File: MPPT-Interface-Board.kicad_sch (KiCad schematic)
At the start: 12 parts, among them J1 MPPT CAN 1, J2 MPPT CAN 2, J3 CarCAN 1, J4 CarCAN 2, J5 FUSEBOX, U1 RI3-1209S

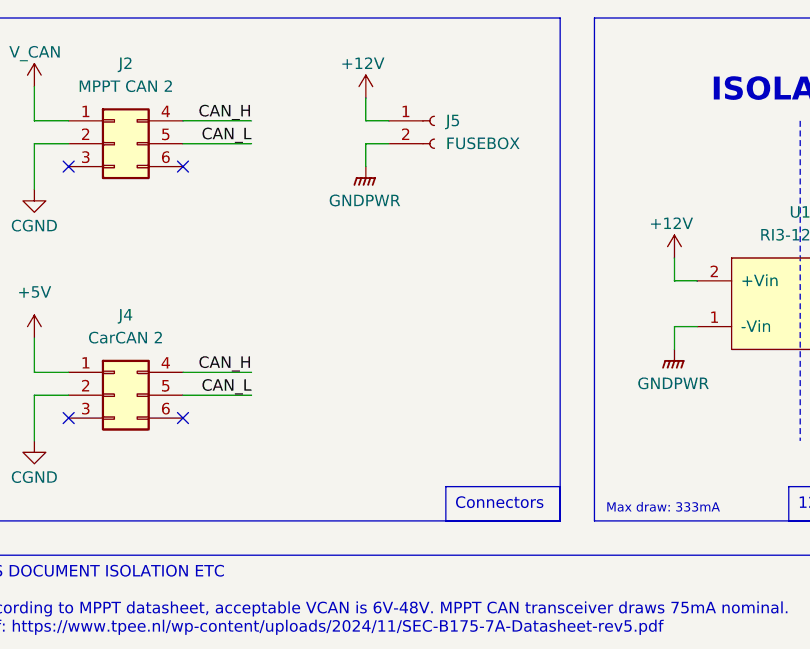
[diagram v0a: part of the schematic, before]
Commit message: add candapter conn
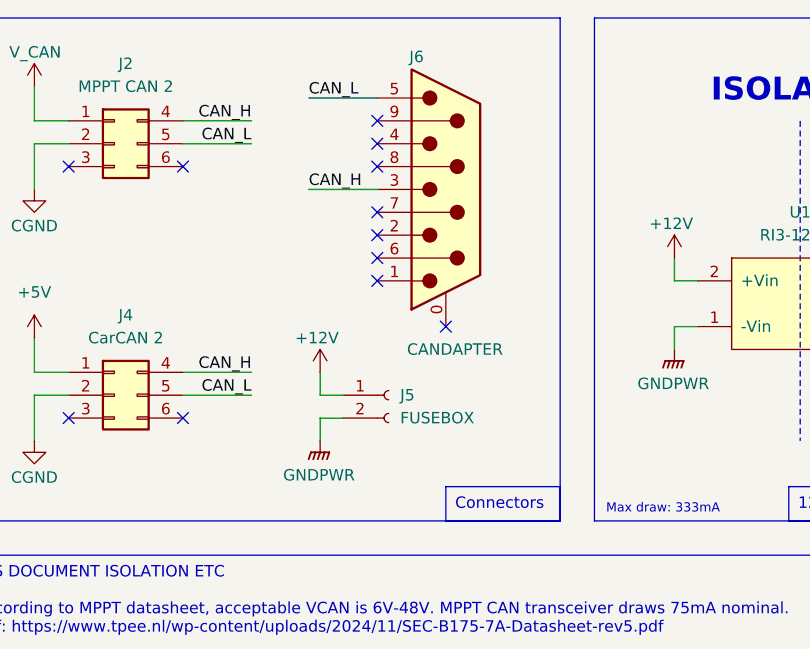
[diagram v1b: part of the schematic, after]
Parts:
- added J6: CANDAPTER, DB-9 Connector:AMPHENOL_L77SDE09SA4CH3R, symbol Connector:DE9_Plug_MountingHoles
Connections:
- net CAN_H: now also J6.3
- net CAN_L: now also J6.5
- no-connect marks 8 -> 16
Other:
- moved on the sheet: J5
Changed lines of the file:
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@@
+	)
+	(no_connect
+		(at 93.98 45.72)
 	)
 	(no_connect
@@
 	)
 	(no_connect
+		(at 93.98 48.26)
+	)
+	(no_connect
 		(at 72.39 63.5)
 	)
@@
 	)
 	(no_connect
+		(at 93.98 33.02)
+	)
+	(no_connect
+		(at 93.98 30.48)
+	)
+	(no_connect
 		(at 27.94 63.5)
 	)
@@
 		(at 40.64 63.5)
 	)
-	(wire
-		(pts
-			(xy 92.71 33.02) (xy 92.71 35.56)
+	(no_connect
+		(at 93.98 43.18)
+	)
+	(no_connect
+		(at 93.98 35.56)
+	)
+	(no_connect
+		(at 93.98 40.64)
+	)
+	(no_connect
+		(at 101.6 53.34)
+	)
+	(wire
+		(pts
+			(xy 87.63 63.5) (xy 87.63 66.04)
 		)
 		(stroke
@@
 	(wire
 		(pts
-			(xy 92.71 30.48) (xy 95.25 30.48)
+			(xy 87.63 60.96) (xy 90.17 60.96)
 		)
 		(stroke
@@
 	(wire
 		(pts
-			(xy 92.71 27.94) (xy 92.71 30.48)
+			(xy 87.63 58.42) (xy 87.63 60.96)
 		)
 		(stroke
@@
 	(wire
 		(pts
+			(xy 86.36 27.94) (xy 93.98 27.94)
+		)
+		(stroke
+			(width 0)
+			(type default)
+		)
+	)
+	(wire
+		(pts
 			(xy 40.64 30.48) (xy 48.26 30.48)
 		)
@@
 	(wire
 		(pts
+			(xy 86.36 38.1) (xy 93.98 38.1)
+		)
+		(stroke
+			(width 0)
+			(type default)
+		)
+	)
+	(wire
+		(pts
 			(xy 222.25 60.96) (xy 222.25 63.5)
 		)
@@
 	(wire
 		(pts
-			(xy 95.25 33.02) (xy 92.71 33.02)
+			(xy 90.17 63.5) (xy 87.63 63.5)
 		)
 		(stroke
@@
 		)
 	)
+	(label "CAN_H"
+		(at 86.36 38.1 0)
+		(fields_autoplaced yes)
+		(effects
+			(font
+				(size 1.27 1.27)
+			)
+			(justify left bottom)
+		)
+	)
 	(label "CAN_L"
 		(at 48.26 60.96 180)
@@
 		)
 	)
+	(label "CAN_L"
+		(at 86.36 27.94 0)
+		(fields_autoplaced yes)
+		(effects
+			(font
+				(size 1.27 1.27)
+			)
+			(justify left bottom)
+		)
+	)
 	(symbol
 		(lib_id "Connector_Generic:Conn_02x03_Top_Bottom")
@@
 	(symbol
 		(lib_id "Connector:Conn_01x02_Socket")
-		(at 100.33 30.48 0)
+		(at 95.25 60.96 0)
 		(unit 1)
 		(exclude_from_sim no)
@@
 		(dnp no)
 		(property "Reference" "J5"
-			(at 101.6 30.4799 0)
+			(at 96.52 60.9599 0)
 			(effects
 				(font
@@
 		)
 		(property "Value" "FUSEBOX"
-			(at 101.6 33.02 0)
+			(at 96.52 63.5 0)
 			(effects
 				(font
@@
 		)
 		(property "Footprint" "Connector_Molex:Molex_Micro-Fit_3.0_43650-0215_1x02_P3.00mm_Vertical"
-			(at 100.33 30.48 0)
+			(at 95.25 60.96 0)
 			(effects
 				(font
@@
 		)
 		(property "Datasheet" "~"
-			(at 100.33 30.48 0)
+			(at 95.25 60.96 0)
 			(effects
 				(font
@@
 		)
 		(property "Description" "Generic connector, single row, 01x02, script generated"
-			(at 100.33 30.48 0)
+			(at 95.25 60.96 0)
 			(effects
 				(font
@@
 		)
 		(property "P/N" "0436500215"
-			(at 100.33 30.48 0)
+			(at 95.25 60.96 0)
 			(effects
 				(font
@@
 		)
 		(property "Sim.Device" ""
-			(at 100.33 30.48 0)
+			(at 95.25 60.96 0)
 			(effects
 				(font
@@
 		)
 		(property "Sim.Pins" ""
-			(at 100.33 30.48 0)
+			(at 95.25 60.96 0)
 			(effects
 				(font
@@
 	)
 	(symbol
+		(lib_id "Connector:DE9_Plug_MountingHoles")
+		(at 101.6 38.1 0)
+		(unit 1)
+		(exclude_from_sim no)
+		(in_bom yes)
+		(on_board yes)
+		(dnp no)
+		(property "Reference" "J6"
+			(at 97.536 23.368 0)
+			(effects
+				(font
+					(size 1.27 1.27)
+				)
+				(justify left)
+			)
+		)
+		(property "Value" "CANDAPTER"
+			(at 97.282 55.88 0)
+			(effects
+				(font
+					(size 1.27 1.27)
+				)
+				(justify left)
+			)
+		)
+		(property "Footprint" "DB-9 Connector:AMPHENOL_L77SDE09SA4CH3R"
+			(at 101.6 38.1 0)
+			(effects
+				(font
+					(size 1.27 1.27)
+				)
+				(hide yes)
+			)
+		)
+		(property "Datasheet" "https://cdn.amphenol-cs.com/media/wysiwyg/files/drawing/l77sdxxxsa4ch3r.pdf"
+			(at 101.6 38.1 0)
+			(effects
+				(font
+					(size 1.27 1.27)
+				)
+				(hide yes)
+			)
+		)
+		(property "Description" "9-pin male plug pin D-SUB connector, Mounting Hole"
+			(at 101.6 38.1 0)
+			(effects
+				(font
+					(size 1.27 1.27)
+				)
+				(hide yes)
+			)
+		)
+		(property "P/N" "L77SDE09SA4CH3R"
+			(at 101.6 38.1 0)
+			(effects
+				(font
+					(size 1.27 1.27)
+				)
+				(hide yes)
+			)
+		)
+		(property "Sim.Device" ""
+			(at 101.6 38.1 0)
+			(effects
+				(font
+					(size 1.27 1.27)
+				)
+				(hide yes)
+			)
+		)
+		(property "Sim.Pins" ""
+			(at 101.6 38.1 0)
+			(effects
+				(font
+					(size 1.27 1.27)
+				)
+				(hide yes)
+			)
+		)
+		(pin "1"
+		)
+		(pin "8"
+		)
+		(pin "2"
+		)
+		(pin "6"
+		)
+		(pin "9"
+		)
+		(pin "7"
+		)
+		(pin "4"
+		)
+		(pin "5"
+		)
+		(pin "3"
+		)
+		(pin "0"
+		)
+		(instances
+			(project "MPPT-Interface-Board"
+				(path "/b7de5949-1fc3-44b6-95a7-0faccc8a2b33"
+					(reference "J6")
+					(unit 1)
+				)
+			)
+		)
+	)
+	(symbol
 		(lib_id "power:GND")
 		(at 24.13 38.1 0)
@@
 	(symbol
 		(lib_id "power:GNDPWR")
-		(at 92.71 35.56 0)
+		(at 87.63 66.04 0)
 		(unit 1)
 		(exclude_from_sim no)
@@
 		(fields_autoplaced yes)
 		(property "Reference" "#PWR02"
-			(at 92.71 40.64 0)
+			(at 87.63 71.12 0)
 			(effects
 				(font
@@
 		)
 		(property "Value" "GNDPWR"
-			(at 92.583 39.37 0)
+			(at 87.503 69.85 0)
 			(effects
 				(font
@@
 		)
 		(property "Footprint" ""
-			(at 92.71 36.83 0)
+			(at 87.63 67.31 0)
 			(effects
 				(font
@@
 		)
 		(property "Datasheet" ""
-			(at 92.71 36.83 0)
+			(at 87.63 67.31 0)
 			(effects
 				(font
@@
 		)
 		(property "Description" "Power symbol creates a global label with name \"GNDPWR\" , global ground"
-			(at 92.71 35.56 0)
+			(at 87.63 66.04 0)
 			(effects
 				(font
@@
 	(symbol
 		(lib_id "power:+12V")
-		(at 92.71 27.94 0)
+		(at 87.63 58.42 0)
 		(unit 1)
 		(exclude_from_sim no)
@@
 		(dnp no)
 		(property "Reference" "#PWR03"
-			(at 92.71 31.75 0)
+			(at 87.63 62.23 0)
 			(effects
 				(font
@@
 		)
 		(property "Value" "+12V"
-			(at 89.916 24.13 0)
+			(at 84.836 54.61 0)
 			(effects
 				(font
@@
 		)
 		(property "Footprint" ""
-			(at 92.71 27.94 0)
+			(at 87.63 58.42 0)
 			(effects
 				(font
@@
 		)
 		(property "Datasheet" ""
-			(at 92.71 27.94 0)
+			(at 87.63 58.42 0)
 			(effects
 				(font
@@
 		)
 		(property "Description" "Power symbol creates a global label with name \"+12V\""
-			(at 92.71 27.94 0)
-			(effects
-				(font
+			(at 87.63 58.42 0)
+			(effects
+				(font

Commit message: add RPP
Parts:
- added C5: 10u, Capacitor_SMD:C_0805_2012Metric, symbol Device:C_Small
- added D1: SD12_SOD323, Diode_SMD:D_SOD-323, symbol Diode:SD12_SOD323
- added Q1: PMV35EPER, Package_TO_SOT_SMD:SOT-23, symbol utsvt-chips:PMV35EPE
- added R2: 100k, Resistor_SMD:R_0805_2012Metric, symbol Device:R_Small
- added Z1: BZT52-B12-QX, Zener:BZT52B12QX, symbol BZT52-B12-QX:BZT52-B12-QX
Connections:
- net +12V: now also D1.2 (A2), Q1.3 (D); no longer U1.2 (+Vin)
- net GNDPWR: now also C5.2, D1.1 (A1), R2.1
- new net: Q1.1 (G), R2.2, Z1.2 (A)
- new net +12V_PROT: C5.1, Q1.2 (S), U1.2 (+Vin), Z1.1 (K)
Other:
- moved on the sheet: C1, C2, C3, C4, U1

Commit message: fix loop?
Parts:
- removed J2: MPPT CAN 2, Connector_Molex:Molex_Micro-Fit_3.0_43045-0612_2x03_P3.00mm_Vertical, symbol Connector_Generic:Conn_02x03_Top_Bottom
- removed J5: FUSEBOX, Connector_Molex:Molex_Micro-Fit_3.0_43650-0215_1x02_P3.00mm_Vertical, symbol Connector:Conn_01x02_Socket
- added J2: MPPT CAN 2, Connector_Molex:Molex_Micro-Fit_3.0_43650-0215_1x02_P3.00mm_Vertical, symbol Connector_Generic:Conn_01x02
- added J5: FUSEBOX, Connector_Molex:Molex_Micro-Fit_3.0_43650-0215_1x02_P3.00mm_Vertical, symbol Connector_Generic:Conn_01x02
- added TP1, TP6: CGND, symbol Connector:TestPoint
- added TP2: GNDPWR, symbol Connector:TestPoint
- added TP3: 5V, symbol Connector:TestPoint
- added TP4: 12V, symbol Connector:TestPoint
- added TP5: VCAN, symbol Connector:TestPoint
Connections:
- net +12V: now also J5.1 (Pin_1)
- net +12V_PROT: now also TP4.1
- net +5V: now also TP3.1
- net CAN_H: now also J2.1 (Pin_1)
- net CAN_L: now also J2.2 (Pin_2)
- net CGND: now also TP1.1, TP6.1
- net GNDPWR: now also J5.2 (Pin_2), TP2.1
- net V_CAN: now also TP5.1
- no-connect marks 16 -> 14

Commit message: add indicator LEDs
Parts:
- added D2: 12V, LED_SMD:LED_0805_2012Metric, symbol Device:LED
- added D3: 5V, LED_SMD:LED_0805_2012Metric, symbol Device:LED
- added D4: VCAN, LED_SMD:LED_0805_2012Metric, symbol Device:LED
- added R3: 22.1k, Resistor_SMD:R_0805_2012Metric, symbol Device:R
- added R4, R5: TODO, Resistor_SMD:R_0805_2012Metric, symbol Device:R
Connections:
- net +12V_PROT: now also R3.1
- net +5V: now also R4.1
- net CGND: now also D3.1 (K), D4.1 (K)
- net GNDPWR: now also D2.1 (K)
- net V_CAN: now also R5.1
- new net: D4.2 (A), R5.2
- new net: D3.2 (A), R4.2
- new net: D2.2 (A), R3.2
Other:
- moved on the sheet: C1, C2, C3, C4, TP1, TP2, TP3, TP4, TP5, TP6

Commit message: more fixes
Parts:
- removed J2: MPPT CAN 2, Connector_Molex:Molex_Micro-Fit_3.0_43650-0215_1x02_P3.00mm_Vertical, symbol Connector_Generic:Conn_01x02
- added J2: MPPT X, Connector_Molex:Molex_Micro-Fit_3.0_43045-0612_2x03_P3.00mm_Vertical, symbol Connector_Generic:Conn_02x03_Top_Bottom
- J1: value MPPT CAN 1 -> MPPT A
- J3: value CarCAN 1 -> CarCAN In
- J4: value CarCAN 2 -> CarCAN Out
- R3: value 22.1k -> 5.1k
- R4: value TODO -> 1.69k
- R5: value TODO -> 3.48k
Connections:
- net CAN_H: no longer J4.4 (Pin_4)
- net CAN_L: no longer J4.5 (Pin_5)
- net CGND: no longer J4.2 (Pin_2)
- net V_CAN: now also J2.1 (Pin_1)
- new net CAN_H2: J2.4 (Pin_4), J4.4 (Pin_4)
- new net CAN_L2: J2.5 (Pin_5), J4.5 (Pin_5)
- new net CGND2: J2.2 (Pin_2), J4.2 (Pin_2)
- no-connect marks 14 -> 16

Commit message: P/N for everything
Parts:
- C1, C2: value 10uF -> 10u
- C3: P/N (none) -> 08053A331JAT2A
- C4: P/N (none) -> 08053C471JAT2A
- C5: P/N C0805C105K3PACTU -> TMK212BBJ106MGHT
- J5: P/N (none) -> 0436500215
- R3: P/N CRCW080522K1FKEA -> RCA08055K10FKEA
- R4: P/N CRCW080522K1FKEA -> CRCW08051K69FKEA
- R5: P/N CRCW080522K1FKEA -> CRCW08053K48FKEA
- U1: P/N (none) -> RI3-1209S
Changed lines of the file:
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@@
 			)
 		)
+		(property "P/N" ""
+			(at 96.52 96.52 0)
+			(effects
+				(font
+					(size 1.27 1.27)
+				)
+				(hide yes)
+			)
+		)
 		(pin "1"
 		)
@@
 			)
 		)
+		(property "P/N" "0436500215"
+			(at 95.25 60.96 0)
+			(effects
+				(font
+					(size 1.27 1.27)
+				)
+				(hide yes)
+			)
+		)
 		(pin "1"
 		)
@@
 			)
 		)
+		(property "P/N" "RI3-1209S"
+			(at 198.12 44.45 0)
+			(effects
+				(font
+					(size 1.27 1.27)
+				)
+				(hide yes)
+			)
+		)
 		(pin "1"
 		)
@@
 			)
 		)
-		(property "P/N" "CRCW080522K1FKEA"
+		(property "P/N" "CRCW08051K69FKEA"
 			(at 139.7 92.71 0)
 			(effects
@@
 			)
 		)
+		(property "P/N" "08053C471JAT2A"
+			(at 210.82 88.9 0)
+			(effects
+				(font
+					(size 1.27 1.27)
+				)
+				(hide yes)
+			)
+		)
 		(pin "2"
 		)
@@
 			)
 		)
-		(property "Value" "10uF"
+		(property "Value" "10u"
 			(at 185.8772 96.393 0)
 			(effects
@@
 			)
 		)
-		(property "Value" "10uF"
+		(property "Value" "10u"
 			(at 174.4472 96.393 0)
 			(effects
@@
 			)
 		)
+		(property "P/N" ""
+			(at 31.75 87.63 0)
+			(effects
+				(font
+					(size 1.27 1.27)
+				)
+				(hide yes)
+			)
+		)
 		(pin "1"
 		)
@@
 			)
 		)
+		(property "P/N" ""
+			(at 86.36 96.52 0)
+			(effects
+				(font
+					(size 1.27 1.27)
+				)
+				(hide yes)
+			)
+		)
 		(pin "1"
 		)
@@
 			)
 		)
+		(property "P/N" ""
+			(at 106.68 96.52 0)
+			(effects
+				(font
+					(size 1.27 1.27)
+				)
+				(hide yes)
+			)
+		)
 		(pin "1"
 		)
@@
 			)
 		)
-		(property "P/N" "CRCW080522K1FKEA"
+		(property "P/N" "RCA08055K10FKEA"
 			(at 128.27 92.71 0)
 			(effects
@@
 			)
 		)
+		(property "P/N" ""
+			(at 73.66 95.25 0)
+			(effects
+				(font
+					(size 1.27 1.27)
+				)
+				(hide yes)
+			)
+		)
 		(pin "1"
 		)
@@
 			)
 		)
+		(property "P/N" ""
+			(at 63.5 95.25 0)
+			(effects
+				(font
+					(size 1.27 1.27)
+				)
+				(hide yes)
+			)
+		)
 		(pin "1"
 		)
@@
 			)
 		)
+		(property "P/N" "08053A331JAT2A"
+			(at 210.82 100.33 0)
+			(effects
+				(font
+					(size 1.27 1.27)
+				)
+				(hide yes)
+			)
+		)
 		(pin "2"
 		)
@@
 			)
 		)
+		(property "P/N" ""
+			(at 53.34 95.25 0)
+			(effects
+				(font
+					(size 1.27 1.27)
+				)
+				(hide yes)
+			)
+		)
 		(pin "1"
 		)
@@
 			)
 		)
-		(property "P/N" "C0805C105K3PACTU"
+		(property "P/N" "TMK212BBJ106MGHT"
 			(at 156.21 46.99 0)
 			(effects
@@
 			)
 		)
-		(property "P/N" "CRCW080522K1FKEA"
+		(property "P/N" "CRCW08053K48FKEA"
 			(at 149.86 92.71 0)
 			(effects

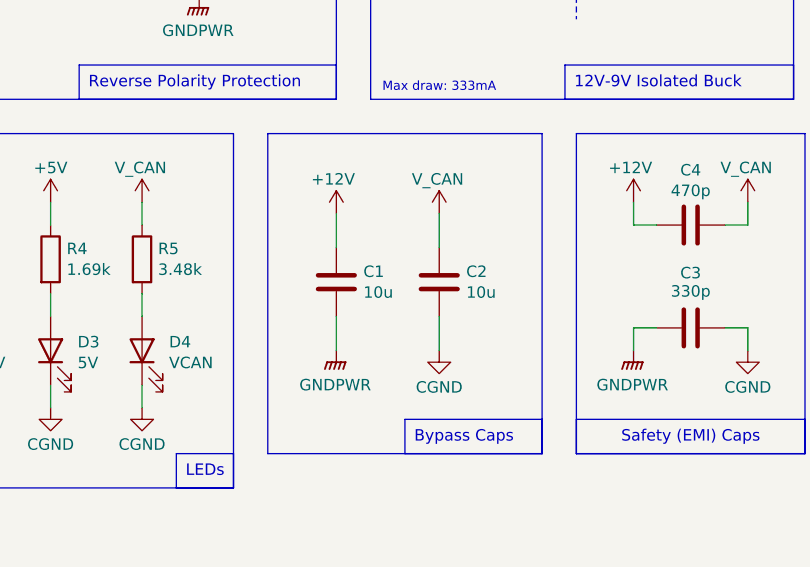
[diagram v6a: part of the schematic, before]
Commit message: fix bypass cap
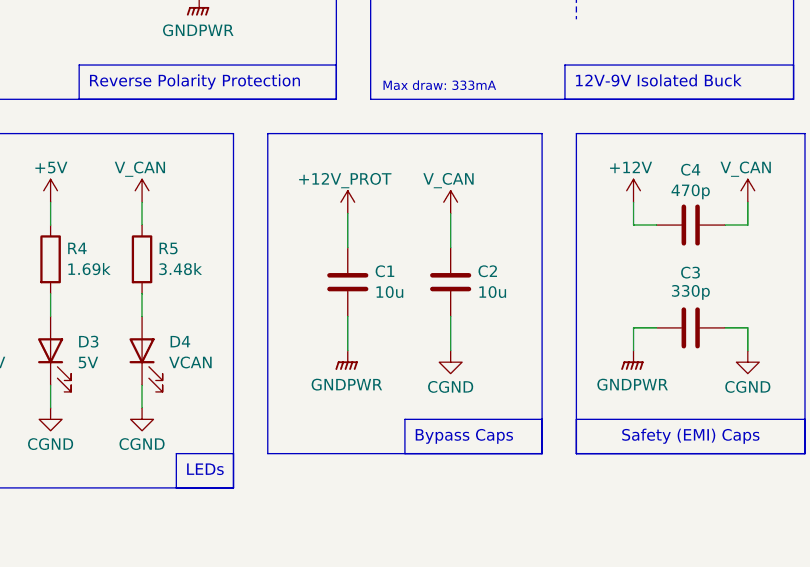
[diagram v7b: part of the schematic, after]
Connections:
- net +12V: no longer C1.1
- net +12V_PROT: now also C1.1
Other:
- moved on the sheet: C1, C2
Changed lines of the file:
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@@
 	(wire
 		(pts
-			(xy 182.88 99.06) (xy 182.88 102.87)
+			(xy 184.15 99.06) (xy 184.15 102.87)
 		)
 		(stroke
@@
 	(wire
 		(pts
-			(xy 171.45 87.63) (xy 171.45 91.44)
+			(xy 172.72 87.63) (xy 172.72 91.44)
 		)
 		(stroke
@@
 	(wire
 		(pts
-			(xy 171.45 99.06) (xy 171.45 102.87)
+			(xy 172.72 99.06) (xy 172.72 102.87)
 		)
 		(stroke
@@
 	(wire
 		(pts
-			(xy 182.88 87.63) (xy 182.88 91.44)
+			(xy 184.15 87.63) (xy 184.15 91.44)
 		)
 		(stroke
@@
 	(symbol
 		(lib_id "power:GNDPWR")
-		(at 171.45 102.87 0)
+		(at 172.72 102.87 0)
 		(unit 1)
 		(exclude_from_sim no)
@@
 		(fields_autoplaced yes)
 		(property "Reference" "#PWR016"
-			(at 171.45 107.95 0)
+			(at 172.72 107.95 0)
 			(effects
 				(font
@@
 		)
 		(property "Value" "GNDPWR"
-			(at 171.323 106.68 0)
+			(at 172.593 106.68 0)
 			(effects
 				(font
@@
 		)
 		(property "Footprint" ""
-			(at 171.45 104.14 0)
+			(at 172.72 104.14 0)
 			(effects
 				(font
@@
 		)
 		(property "Datasheet" ""
-			(at 171.45 104.14 0)
+			(at 172.72 104.14 0)
 			(effects
 				(font
@@
 		)
 		(property "Description" "Power symbol creates a global label with name \"GNDPWR\" , global ground"
-			(at 171.45 102.87 0)
+			(at 172.72 102.87 0)
 			(effects
 				(font
@@
 	(symbol
 		(lib_id "Device:C")
-		(at 182.88 95.25 0)
+		(at 184.15 95.25 0)
 		(unit 1)
 		(exclude_from_sim no)
@@
 		(dnp no)
 		(property "Reference" "C2"
-			(at 185.8772 94.0816 0)
+			(at 187.1472 94.0816 0)
 			(effects
 				(font
@@
 		)
 		(property "Value" "10u"
-			(at 185.8772 96.393 0)
+			(at 187.1472 96.393 0)
 			(effects
 				(font
@@
 		)
 		(property "Footprint" "Capacitor_SMD:C_0805_2012Metric"
-			(at 183.8452 99.06 0)
+			(at 185.1152 99.06 0)
 			(effects
 				(font
@@
 		)
 		(property "Datasheet" "~"
-			(at 182.88 95.25 0)
+			(at 184.15 95.25 0)
 			(effects
 				(font
@@
 		)
 		(property "Description" "Unpolarized capacitor"
-			(at 182.88 95.25 0)
+			(at 184.15 95.25 0)
 			(effects
 				(font
@@
 		)
 		(property "P/N" "TMK212BBJ106MGHT"
-			(at 182.88 95.25 0)
+			(at 184.15 95.25 0)
 			(effects
 				(font
@@
 		)
 		(property "Mouser Part Number" "581-22201C106KAT2A"
-			(at 182.88 95.25 0)
+			(at 184.15 95.25 0)
 			(effects
 				(font
@@
 		)
 		(property "PN" ""
-			(at 182.88 95.25 0)
+			(at 184.15 95.25 0)
 			(effects
 				(font
@@
 		)
 		(property "p/n" ""
-			(at 182.88 95.25 0)
+			(at 184.15 95.25 0)
 			(effects
 				(font
@@
 	(symbol
 		(lib_id "power:GND")
-		(at 182.88 102.87 0)
+		(at 184.15 102.87 0)
 		(unit 1)
 		(exclude_from_sim no)
@@
 		(dnp no)
 		(property "Reference" "#PWR018"
-			(at 182.88 109.22 0)
+			(at 184.15 109.22 0)
 			(effects
 				(font
@@
 		)
 		(property "Value" "CGND"
-			(at 182.88 106.934 0)
+			(at 184.15 106.934 0)
 			(effects
 				(font
@@
 		)
 		(property "Footprint" ""
-			(at 182.88 102.87 0)
+			(at 184.15 102.87 0)
 			(effects
 				(font
@@
 		)
 		(property "Datasheet" ""
-			(at 182.88 102.87 0)
+			(at 184.15 102.87 0)
 			(effects
 				(font
@@
 		)
 		(property "Description" "Power symbol creates a global label with name \"GND\" , ground"
-			(at 182.88 102.87 0)
+			(at 184.15 102.87 0)
 			(effects
 				(font
@@
 	(symbol
 		(lib_id "Device:C")
-		(at 171.45 95.25 0)
+		(at 172.72 95.25 0)
 		(unit 1)
 		(exclude_from_sim no)
@@
 		(dnp no)
 		(property "Reference" "C1"
-			(at 174.4472 94.0816 0)
+			(at 175.7172 94.0816 0)
 			(effects
 				(font
@@
 		)
 		(property "Value" "10u"
-			(at 174.4472 96.393 0)
+			(at 175.7172 96.393 0)
 			(effects
 				(font
@@
 		)
 		(property "Footprint" "Capacitor_SMD:C_0805_2012Metric"
-			(at 172.4152 99.06 0)
+			(at 173.6852 99.06 0)
 			(effects
 				(font
@@
 		)
 		(property "Datasheet" "~"
-			(at 171.45 95.25 0)
+			(at 172.72 95.25 0)
 			(effects
 				(font
@@
 		)
 		(property "Description" "Unpolarized capacitor"
-			(at 171.45 95.25 0)
+			(at 172.72 95.25 0)
 			(effects
 				(font
@@
 		)
 		(property "P/N" "TMK212BBJ106MGHT"
-			(at 171.45 95.25 0)
+			(at 172.72 95.25 0)
 			(effects
 				(font
@@
 		)
 		(property "Mouser Part Number" "581-22201C106KAT2A"
-			(at 171.45 95.25 0)
+			(at 172.72 95.25 0)
 			(effects
 				(font
@@
 		)
 		(property "PN" ""
-			(at 171.45 95.25 0)
+			(at 172.72 95.25 0)
 			(effects
 				(font
@@
 		)
 		(property "p/n" ""
-			(at 171.45 95.25 0)
+			(at 172.72 95.25 0)
 			(effects
 				(font
@@
 	(symbol
 		(lib_id "power:+12V")
-		(at 182.88 87.63 0)
+		(at 184.15 87.63 0)
 		(unit 1)
 		(exclude_from_sim no)
@@
 		(dnp no)
 		(property "Reference" "#PWR017"
-			(at 182.88 91.44 0)
+			(at 184.15 91.44 0)
 			(effects
 				(font
@@
 		)
 		(property "Value" "V_CAN"
-			(at 179.832 83.82 0)
+			(at 181.102 83.82 0)
 			(effects
 				(font
@@
 		)
 		(property "Footprint" ""
-			(at 182.88 87.63 0)
+			(at 184.15 87.63 0)
 			(effects
 				(font
@@
 		)
 		(property "Datasheet" ""
-			(at 182.88 87.63 0)
+			(at 184.15 87.63 0)
 			(effects
 				(font
@@
 		)
 		(property "Description" "Power symbol creates a global label with name \"+12V\""
-			(at 182.88 87.63 0)
+			(at 184.15 87.63 0)
 			(effects
 				(font
@@
 	(symbol
 		(lib_id "power:+12V")
-		(at 171.45 87.63 0)
+		(at 172.72 87.63 0)
 		(unit 1)
 		(exclude_from_sim no)
@@
 		(dnp no)
 		(property "Reference" "#PWR015"
-			(at 171.45 91.44 0)
+			(at 172.72 91.44 0)
 			(effects
 				(font
@@
 			)
 		)
-		(property "Value" "+12V"
-			(at 168.656 83.82 0)
+		(property "Value" "+12V_PROT"
+			(at 167.132 83.82 0)
 			(effects
 				(font
@@
 		)
 		(property "Footprint" ""
-			(at 171.45 87.63 0)
+			(at 172.72 87.63 0)
 			(effects
 				(font
@@
 		)
 		(property "Datasheet" ""
-			(at 171.45 87.63 0)
+			(at 172.72 87.63 0)
 			(effects
 				(font
@@
 		)
 		(property "Description" "Power symbol creates a global label with name \"+12V\""
-			(at 171.45 87.63 0)
+			(at 172.72 87.63 0)
 			(effects
 				(font
